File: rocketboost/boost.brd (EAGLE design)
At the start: 65 x 30 mm, 16 parts, among them U1 TPS61232DRCR

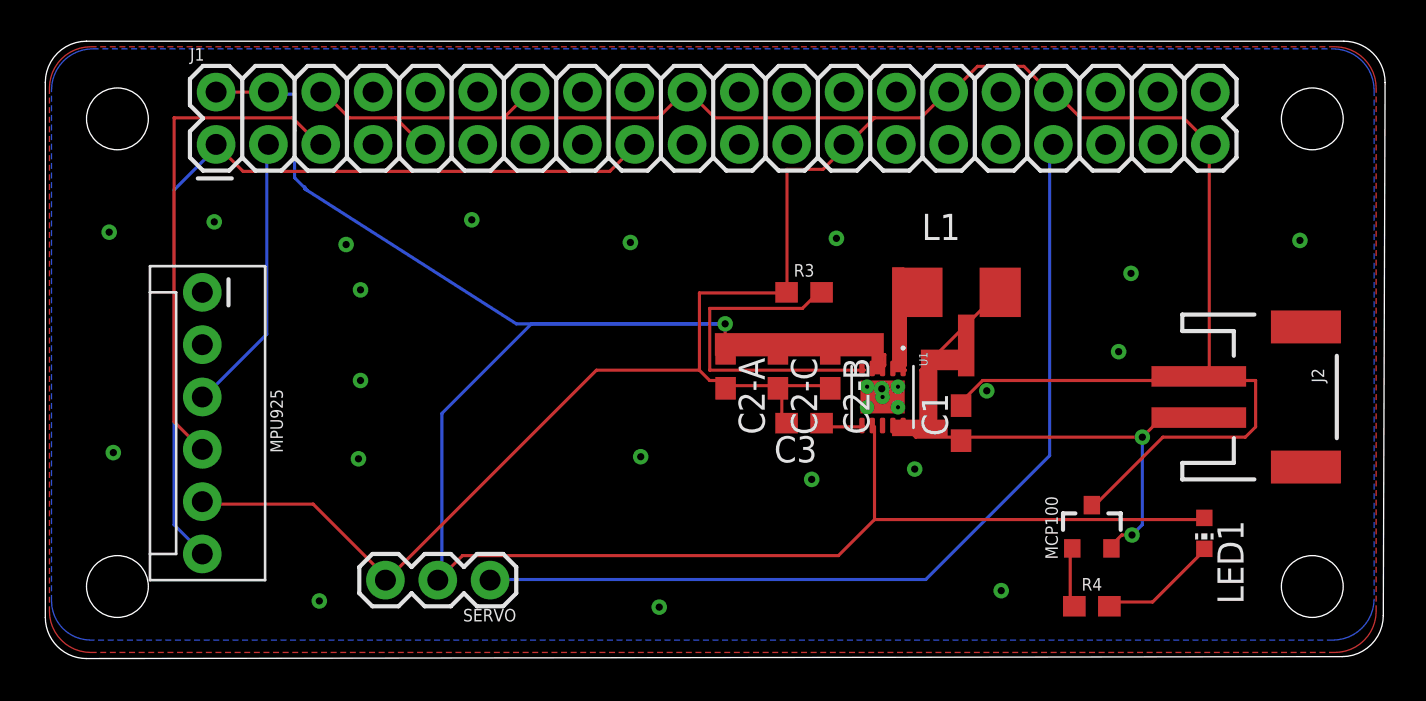
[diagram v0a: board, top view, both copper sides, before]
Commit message: board with ground proper to 61232
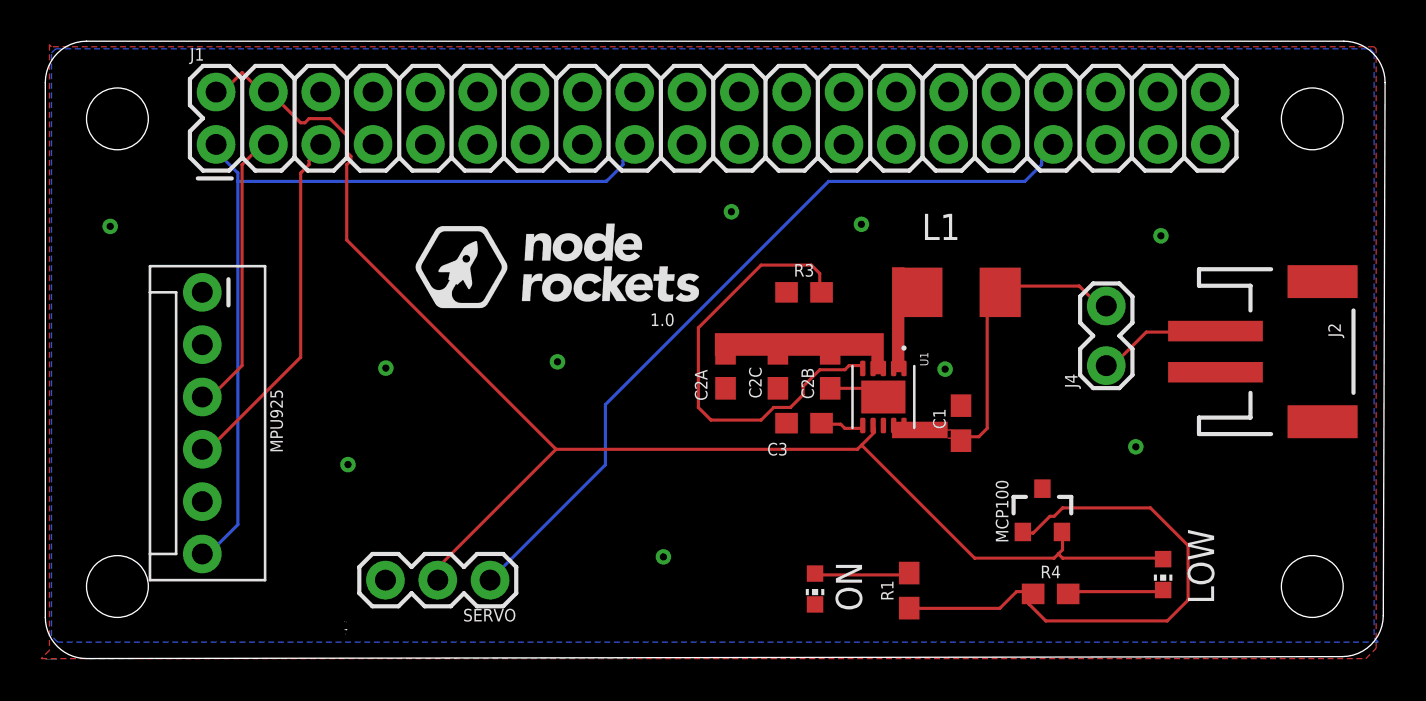
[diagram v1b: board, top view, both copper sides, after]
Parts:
- removed DRILEGEND: (no value), drilegend:DRILEGEND
- removed LED1: (no value), led:CHIP-LED0603
- added J4: (no value), SparkFun-Connectors:1X02_LOCK
- added LOW, ON: -+, led:CHIP-LED0603
- added R1: 3.3k, SparkFun-Resistors:0603
- C2A, C2B, C2C: value 22uF -> 22u
- U1: value TPS61232DRCR -> TI61232; device TPS61232DRCR:SON50P300X300X100-10N -> TPS61232DRCR-1:SON50P300X300X100-10N
- moved MCP100 2.53 mm to (48.4, 7.15)
- moved J2 2.34 mm to (60.5, 14.9)
- moved R4 2.09 mm to (48.8, 3.14)
- renumbered C2-A to C2A, C2-B to C2B, C2-C to C2C
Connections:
- net N$9 renamed PWM
- removed net VOUT2: U1.4
- new net N$1: J2.1, J4.1
- new net N$2: ON.A, R1.2
- net GND: now also J2.2, ON.C; no longer J2.1
- net N$13: now also LOW.C; no longer LED1.C
- net N$4: now also R1.1
- net VIN: now also J4.2; no longer J2.2, MCP100.2
- net VOUT: now also LOW.A, MCP100.2, U1.4; no longer LED1.A
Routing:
- net GND: track 148.3 -> 1.97 mm, vias 19 -> 10
- net VOUT: track 108.1 -> 71.0 mm, vias 1 -> 0
- net N$4: track 2.93 -> 27.4 mm
- net VIN: track 31.1 -> 14.1 mm, vias 2 -> 0
- net SCL: track 24.3 -> 17.4 mm
- net PWM: track 44.8 -> 38.1 mm
- net N$1: track 0.00 -> 5.98 mm
- net PG: track 16.4 -> 21.8 mm
- net SW: track 5.28 -> 0.00 mm
- net N$2: track 0.00 -> 4.66 mm
- net N$13: track 5.85 -> 4.72 mm
- net V33: track 42.7 -> 41.6 mm
- added copper zone on layer 1, net VIN
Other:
- board text added: "/Users/olsonsd/Downloads/node-rockets.BMP"
- board text added: "1.0"
- board text added: "BLACK (-)"
- board text added: "GND 5V PWM"
- board text added: "RED (+)"
- board text added: "SDA SCL GND 3.3V"
- board text removed: "01-16"
- board text removed: "01-20"
- board text removed: "LAYER-STACK"

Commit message: ver 2.0
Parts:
- removed C2B, C2C: 22u, rcl:C0603
- removed J4: (no value), SparkFun-Connectors:1X02_LOCK
- removed LOW, ON: -+, led:CHIP-LED0603
- added C2-B, C2-C: 22uF, rcl:C0603
- added J3: SWITCH, SparkFun-Connectors:1X02
- added LED1: LO, led:CHIP-LED0603
- added LED2: ok, led:CHIP-LED0603
- C2-A: value 22u -> 22uF
- J2: value (none) -> PWR
- U1: value TI61232 -> TPS61232DRCR; device TPS61232DRCR-1:SON50P300X300X100-10N -> steveo:SON50P300X300X100-10N
- moved R1 3.93 mm to (43.9, 6.70), turned to 0 degrees
- moved MCP100 2.83 mm to (50.3, 9.25)
- moved J2 2.34 mm to (59.7, 12.7)
- moved R4 1.82 mm to (50.6, 3.44)
- moved U1 0.30 mm to (40.7, 12.4)
- renumbered C2A to C2-A, MPU925 to 3.3-GND-SCL-SDA, SERVO to GND-5.0-PWM
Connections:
- net PWM renamed N$9
- removed net N$2: ON.A, R1.2
- new net N$22: J2.1, J3.2
- net GND: now also C2-B.2, C2-C.2, R1.1; no longer C2B.2, C2C.2, ON.C
- net N$1: now also LED2.C, R1.2; no longer J2.1, J4.1
- net N$13: now also LED1.C; no longer LOW.C
- net N$4: now also LED2.A; no longer R1.1
- net VIN: now also J3.1; no longer J4.2
- net VOUT: now also C2-B.1, C2-C.1, LED1.A; no longer C2B.1, C2C.1, LOW.A
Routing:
- net VOUT: track 71.0 -> 93.7 mm, vias 0 -> 2
- net N$4: track 27.4 -> 7.19 mm
- net N$22: track 0.00 -> 6.54 mm
- net VIN: track 14.1 -> 20.5 mm
- net PG: track 21.8 -> 27.8 mm
- net SW: track 0.00 -> 4.85 mm
- net N$2: track 4.66 -> 0.00 mm
- net SCL: track 17.4 -> 20.9 mm
- net N$9: track 38.1 -> 41.5 mm
- net V33: track 41.6 -> 44.9 mm
- net N$1: track 5.98 -> 3.78 mm
- net GND: track 1.97 -> 0.00 mm, vias 10 -> 14
- net N$13: track 4.72 -> 2.91 mm
- net SDA: track 14.1 -> 15.0 mm
- removed copper zone on layer 1, net VIN
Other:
- outline, holes or cut-outs redrawn
- board text added: "/Users/olsonsd/Documents/EAGLE/projects/rocketboost/node-rockets.BMP"
- board text added: "2.0"
- board text removed: "/Users/olsonsd/Downloads/node-rockets.BMP"
- board text removed: "1.0"
- board text removed: "BLACK (-)"
- board text removed: "GND 5V PWM"
- board text removed: "RED (+)"
- board text removed: "SDA SCL GND 3.3V"
